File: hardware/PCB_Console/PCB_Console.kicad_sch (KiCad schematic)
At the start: 52 parts, among them J1 USB_C_Receptacle_PowerOnly_6P, J2 CP2102 module, Q1 2N3904, U1 LD1117S33TR_SOT223, U2 IP5306, U3 ESP32-WROOM-32

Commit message: dodano przyciski, poprawione biblioteki
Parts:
- removed DWN_SWCH1, ON_OFF_SWITCH1, RESET_SWCH1: SW_Push_Dual, Library:SW_Push_12x12_aliexpress, symbol Switch:SW_Push_Dual
- added C_SW3, C_SW4, C_SW5, C_SW6, C_SW7, C_SW8: 100n, Capacitor_SMD:C_1206_3216Metric_Pad1.33x1.80mm_HandSolder, symbol Device:C
- added SW1, SW2, SW3, SW4, SW5, SW6, SW7, SW8, SW9: SW_MEC_5E, Library:SW_Push_12x12_aliexpress, symbol Switch:SW_MEC_5E
- U2: footprint IP5306:SOIC9P127_490X600X170L84X42T330X241N -> components_lib:SOIC9P127_490X600X170L84X42T330X241N
- U4: footprint ASK:TFT ILI9341 -> components_lib:TFT ILI9341
- renumbered H1 to BAT+1, H2 to BAT-1, R6 to R10, R7 to R6, R8 to R7, R9 to R8, R10 to R9
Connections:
- net EN_ESP: now also SW2.3 (K), SW2.4 (A)
- net GND: now also C_SW3.1, C_SW4.1, C_SW5.1, C_SW6.1, C_SW7.1, C_SW8.1, SW1.1, SW1.2, SW2.1, SW2.2, SW3.3 (K), SW3.4 (A), SW4.3 (K), SW4.4 (A), SW5.3 (K), SW5.4 (A), SW6.3 (K), SW6.4 (A), SW7.3 (K), SW7.4 (A), SW8.3 (K), SW8.4 (A), SW9.3 (K), SW9.4 (A)
- net GPIO0: now also SW1.3 (K), SW1.4 (A)
- net at R4.1: now also SW9.1, SW9.2
- net IO25_B: now reaches U3.10 (IO25)
- net IO25_B: now also C_SW7.2, SW7.1, SW7.2
- net IO26_B: now reaches U3.11 (IO26)
- net IO26_B: now also C_SW6.2, SW6.1, SW6.2
- net IO27_B: now reaches U3.12 (IO27)
- net IO27_B: now also C_SW5.2, SW5.1, SW5.2
- net IO14_B: now reaches U3.13 (IO14)
- net IO14_B: now also C_SW8.2, SW8.1, SW8.2
- net IO32_B: now reaches U3.8 (IO32)
- net IO32_B: now also C_SW3.2, SW3.1, SW3.2
- net IO33_B: now reaches U3.9 (IO33)
- net IO33_B: now also C_SW4.2, SW4.1, SW4.2

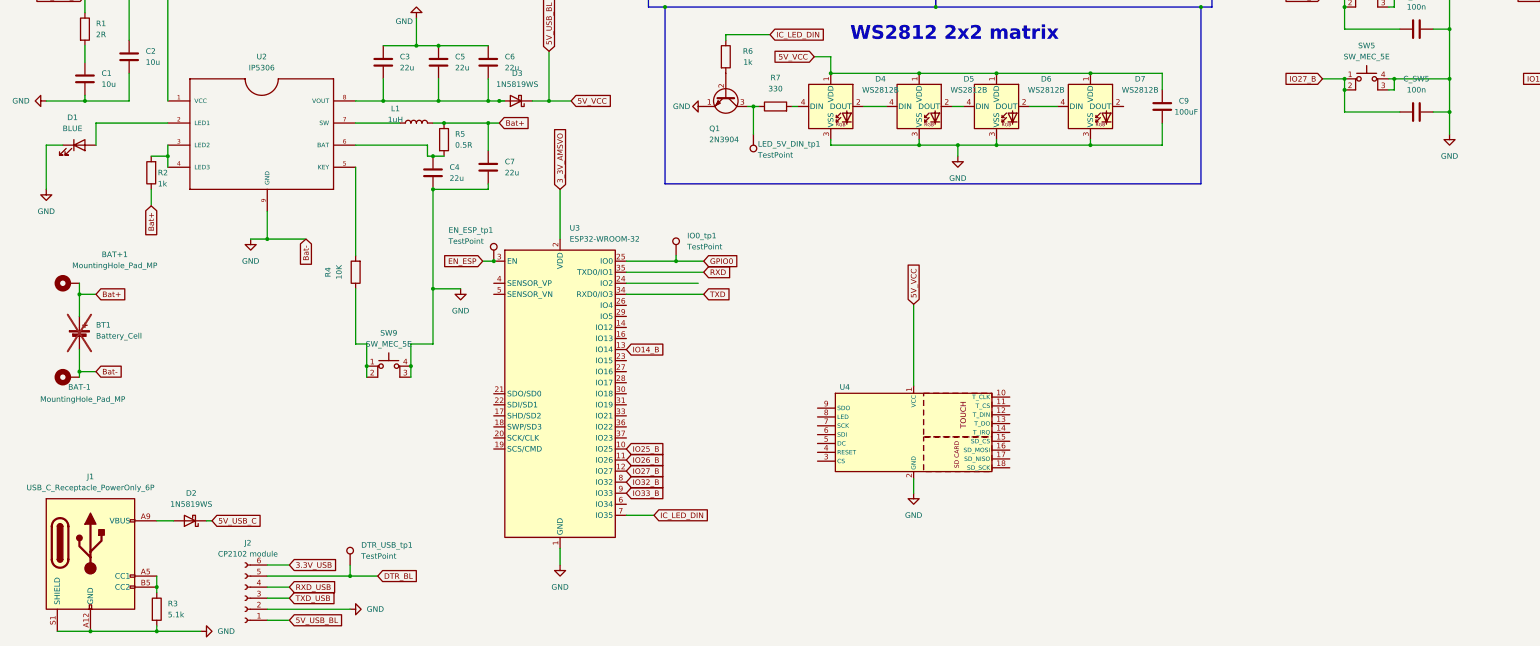
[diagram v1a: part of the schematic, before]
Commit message: display connected to esp, pinout checked
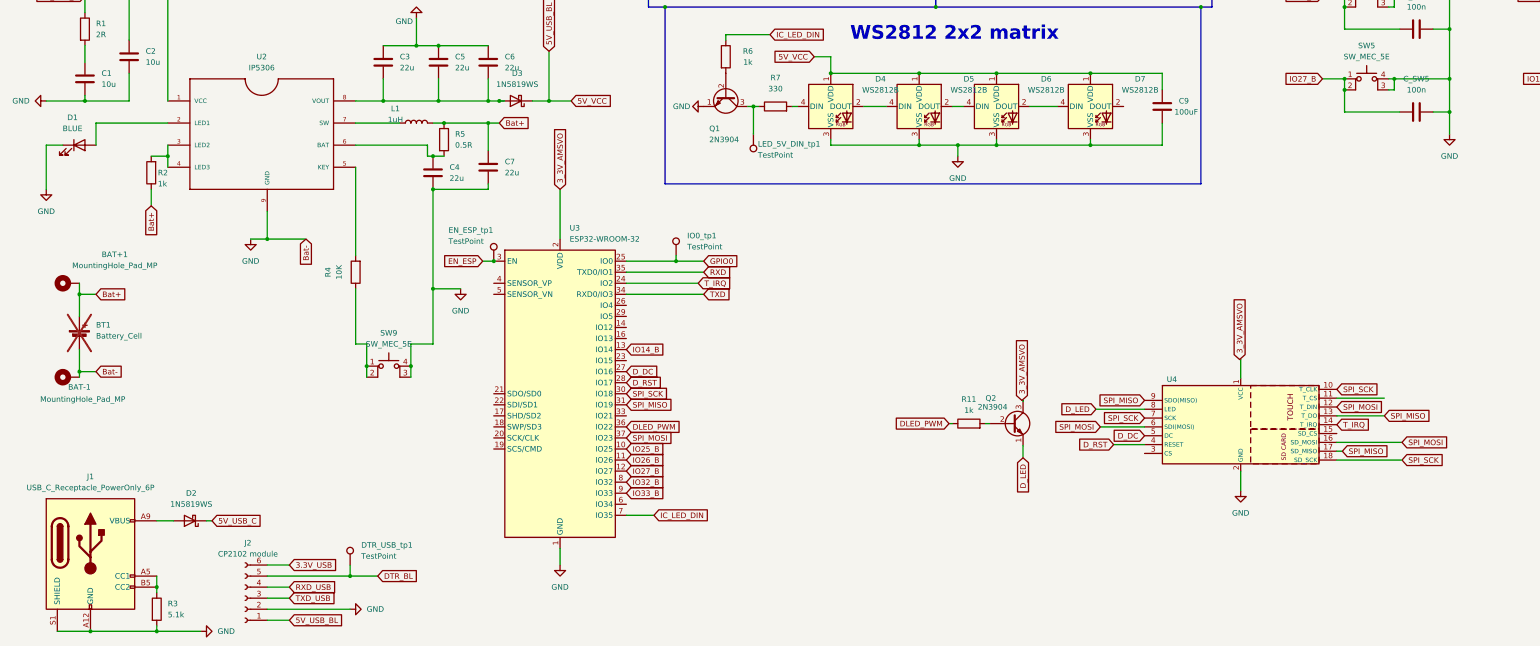
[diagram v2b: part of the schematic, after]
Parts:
- added Q2: 2N3904, Package_TO_SOT_THT:TO-92_Wide, symbol Transistor_BJT:2N3904
- added R11: 1k, symbol Device:R
- BAT+1, BAT-1: now in the parts list
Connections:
- net 3_3V_AMSVO: now also U4.1 (VCC), Q2.3 (C)
- net 5V_USB_BL: no longer U4.1 (VCC)
- net SPI_SCK: now reaches U4.10 (T_CLK)
- net SPI_SCK: now also U3.30 (IO18), U4.18 (SD_SCK), U4.7 (SCK)
- net SPI_MOSI: now reaches U4.12 (T_DIN)
- net SPI_MOSI: now also U3.37 (IO23), U4.16 (SD_MOSI), U4.6 (SDI(MOSI))
- net SPI_MISO: now reaches U4.13 (T_DO)
- net SPI_MISO: now also U3.31 (IO19), U4.17 (SD_MISO), U4.9 (SDO(MISO))
- net T_IRQ: now reaches U4.14 (T_IRQ)
- net T_IRQ: now also U3.24 (IO2)
- net D_RST: now reaches U4.4 (RESET)
- net D_RST: now also U3.28 (IO17)
- net D_DC: now reaches U4.5 (DC)
- net D_DC: now also U3.27 (IO16)
- net D_LED: now reaches U4.8 (LED)
- net D_LED: now also Q2.1 (E)
- net DLED_PWM: now reaches U3.36 (IO22)
- net DLED_PWM: now also R11.1
- new net: Q2.2 (B), R11.2
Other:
- moved on the sheet: U4

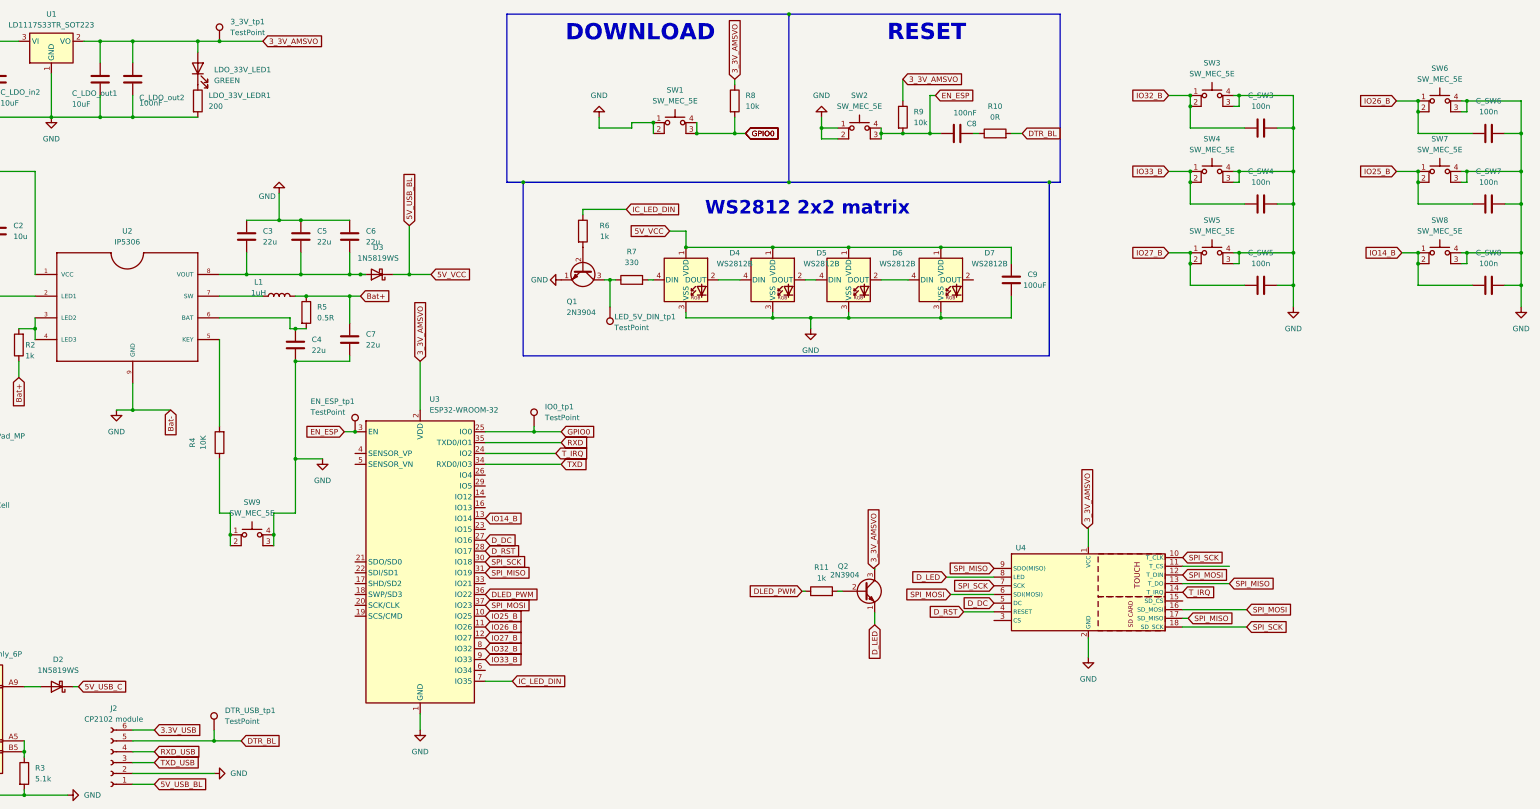
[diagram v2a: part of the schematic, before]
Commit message: display connected to esp, pinout checked
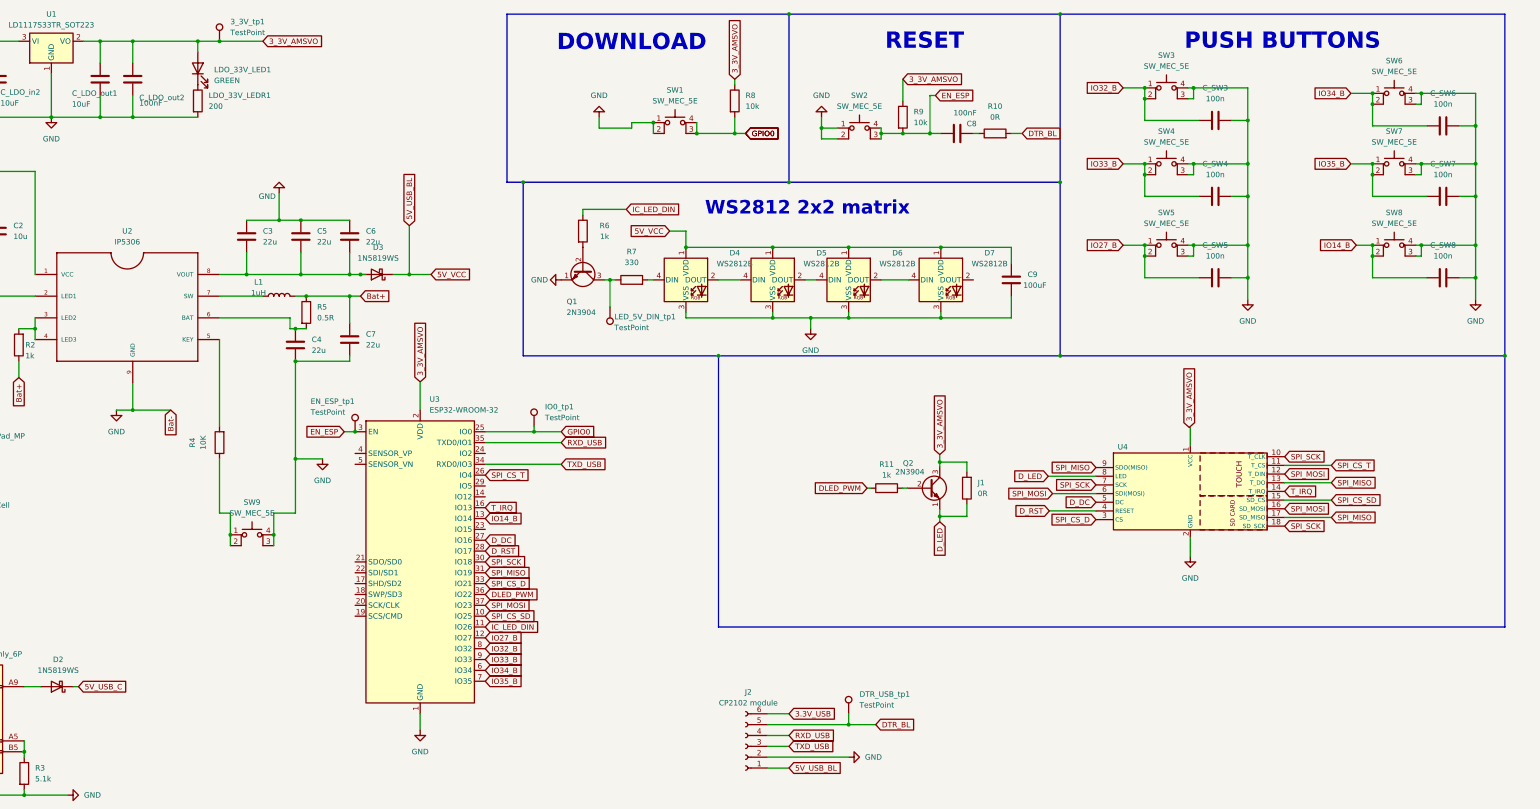
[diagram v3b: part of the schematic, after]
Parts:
- added J1: 0R, Resistor_SMD:R_1206_3216Metric_Pad1.30x1.75mm_HandSolder, symbol Device:R
- D1: footprint (none) -> LED_THT:LED_D5.0mm
- R11: footprint (none) -> Resistor_SMD:R_1206_3216Metric_Pad1.30x1.75mm_HandSolder
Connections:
- net RXD is gone; now on net RXD_USB: U3.35 (TXD0/IO1)
- net TXD is gone; now on net TXD_USB: U3.34 (RXD0/IO3)
- net 3_3V_AMSVO: now also J1.2
- net D_LED: now also J1.1
- net IC_LED_DIN: now also U3.11 (IO26); no longer U3.7 (IO35)
- net T_IRQ: now also U3.16 (IO13); no longer U3.24 (IO2)
- net SPI_CS_T: now reaches U4.11 (T_CS)
- net SPI_CS_T: now also U3.26 (IO4)
- net SPI_CS_SD: now reaches U4.15 (SD_CS)
- net SPI_CS_SD: now also U3.10 (IO25)
- net SPI_CS_D: now reaches U4.3 (CS)
- net SPI_CS_D: now also U3.33 (IO21)
- net IO34_B: now reaches U3.6 (IO34)
- net IO34_B: now also C_SW6.2, SW6.1, SW6.2
- net IO25_B renamed IO35_B
- net IO35_B: now also U3.7 (IO35); no longer U3.10 (IO25)
- removed net IO26_B: C_SW6.2, SW6.1, SW6.2, U3.11 (IO26)
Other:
- note added: "PUSH BUTTONS"
- moved on the sheet: C_SW3, C_SW4, C_SW5, C_SW6, C_SW7, C_SW8, DTR_USB_tp1, J2, Q2, R11, SW3, SW4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

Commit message: deleted unnecessery back-ups; making schematic more modular, easier to read
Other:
- note added: "BOOTLOAD SOCKET"
- note added: "TFT 2.8" DISPLAY"
- moved on the sheet: 3_3V_tp1, BAT+1, BAT-1, BT1, C_LDO_in1, C_LDO_in2, C_LDO_out1, C_LDO_out2, D2, DTR_USB_tp1, EN_ESP_tp1, IO0_tp1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
